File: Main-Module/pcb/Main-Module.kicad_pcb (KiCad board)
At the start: 4 copper layers, 83.9 x 50 mm, 49 parts, among them J1 Conn_02x10_Odd_Even, SW1 SW_DIP_x03, U1 W25Q128JVS, U2 MCP130-xxxxTT, U3 STM32H503RBTx, U5 MCP73831-2-MC, U6 MS5607-02BA, U7 ADXL375BCCZ

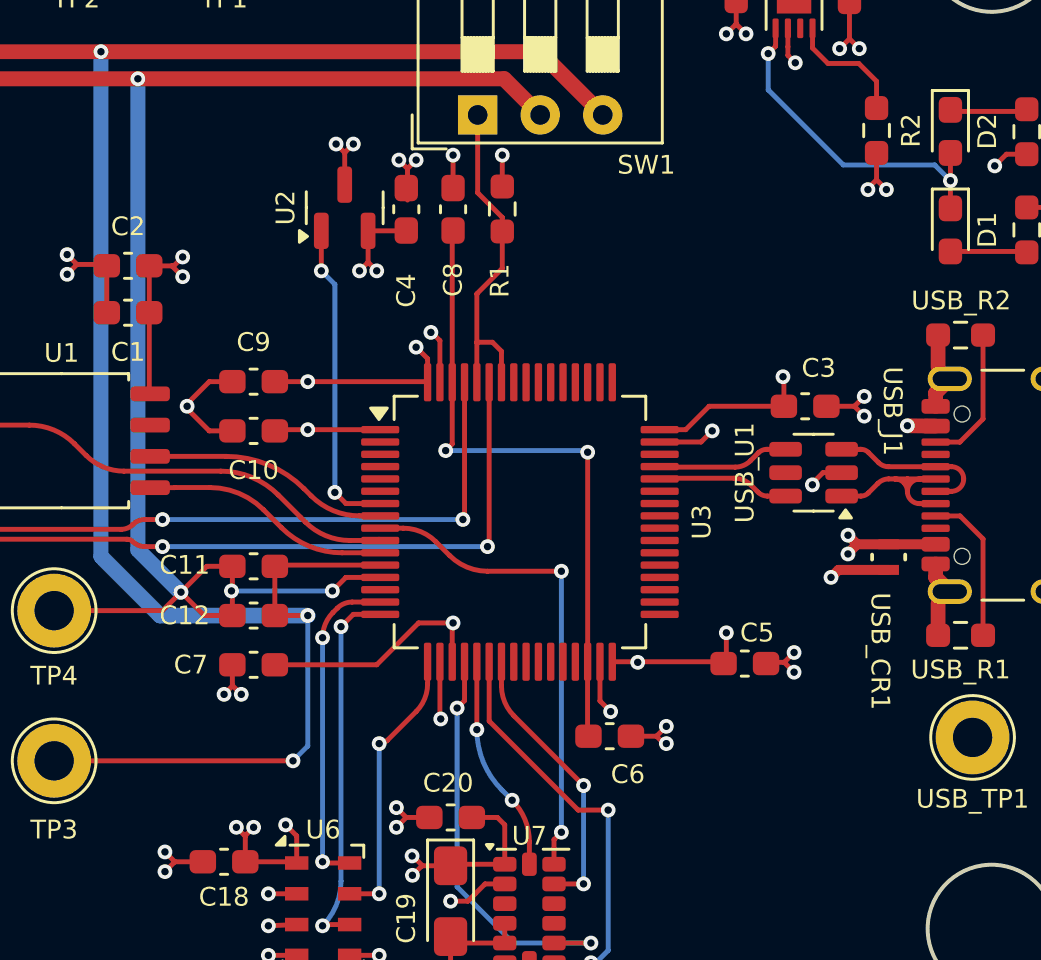
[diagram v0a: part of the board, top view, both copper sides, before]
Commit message: Minor routing changes
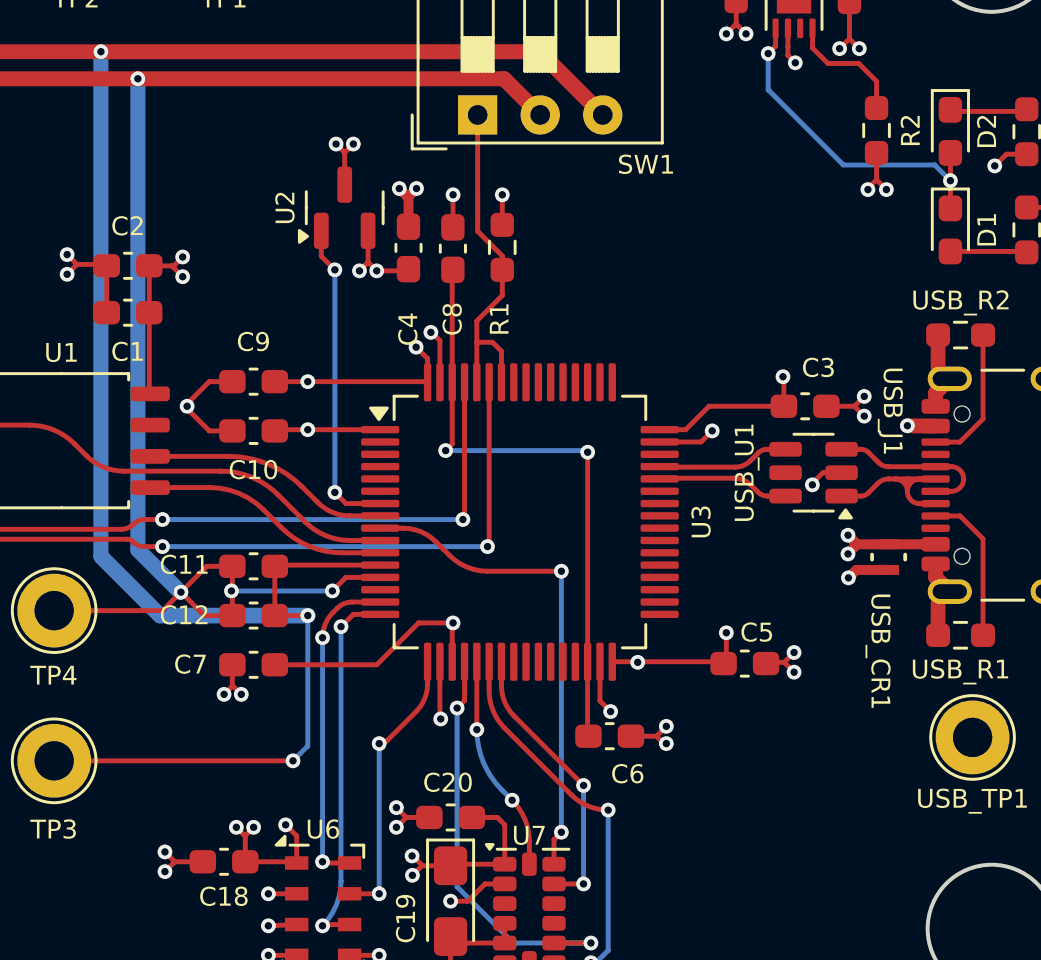
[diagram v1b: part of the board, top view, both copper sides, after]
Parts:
- moved C8 1.60 mm to (159.9, 102.9)
- moved C4 1.57 mm to (158.1, 102.9)
- moved R1 1.56 mm to (161.9, 102.8)
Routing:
- net Net-(C6-Pad1): track 26.8 -> 25.1 mm
